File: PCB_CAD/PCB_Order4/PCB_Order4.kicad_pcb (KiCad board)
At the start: 4 copper layers, 150 x 130 mm, 95 parts

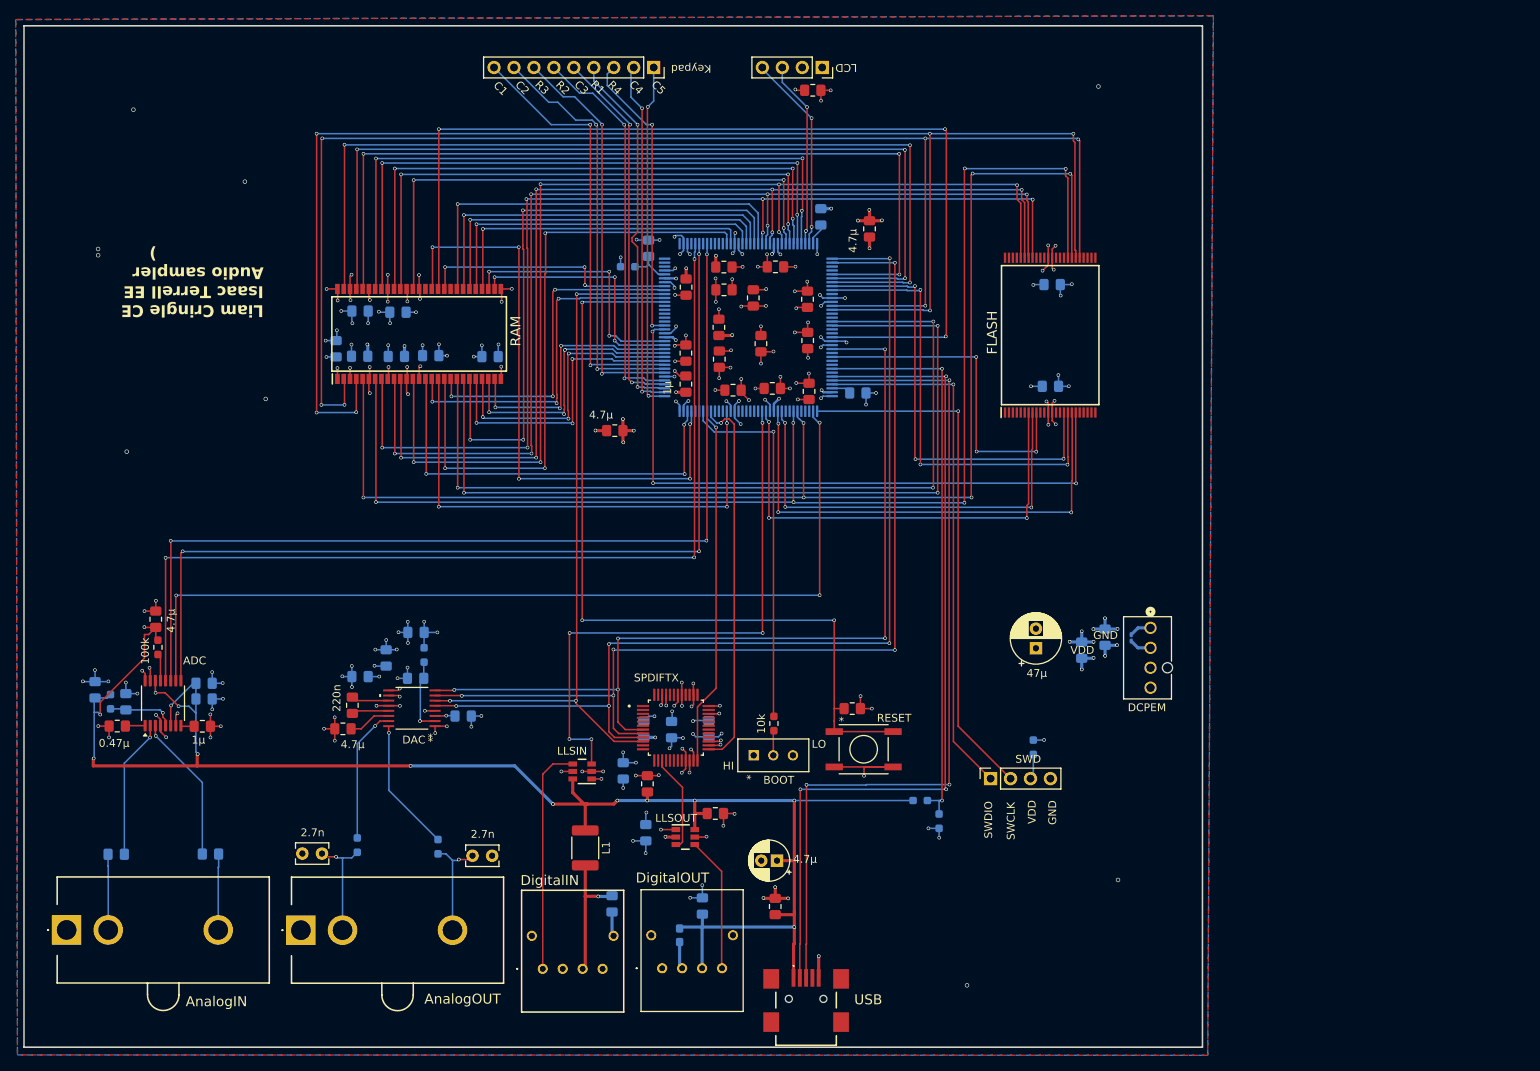
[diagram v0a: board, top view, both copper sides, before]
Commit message: more work on USB and Toslink
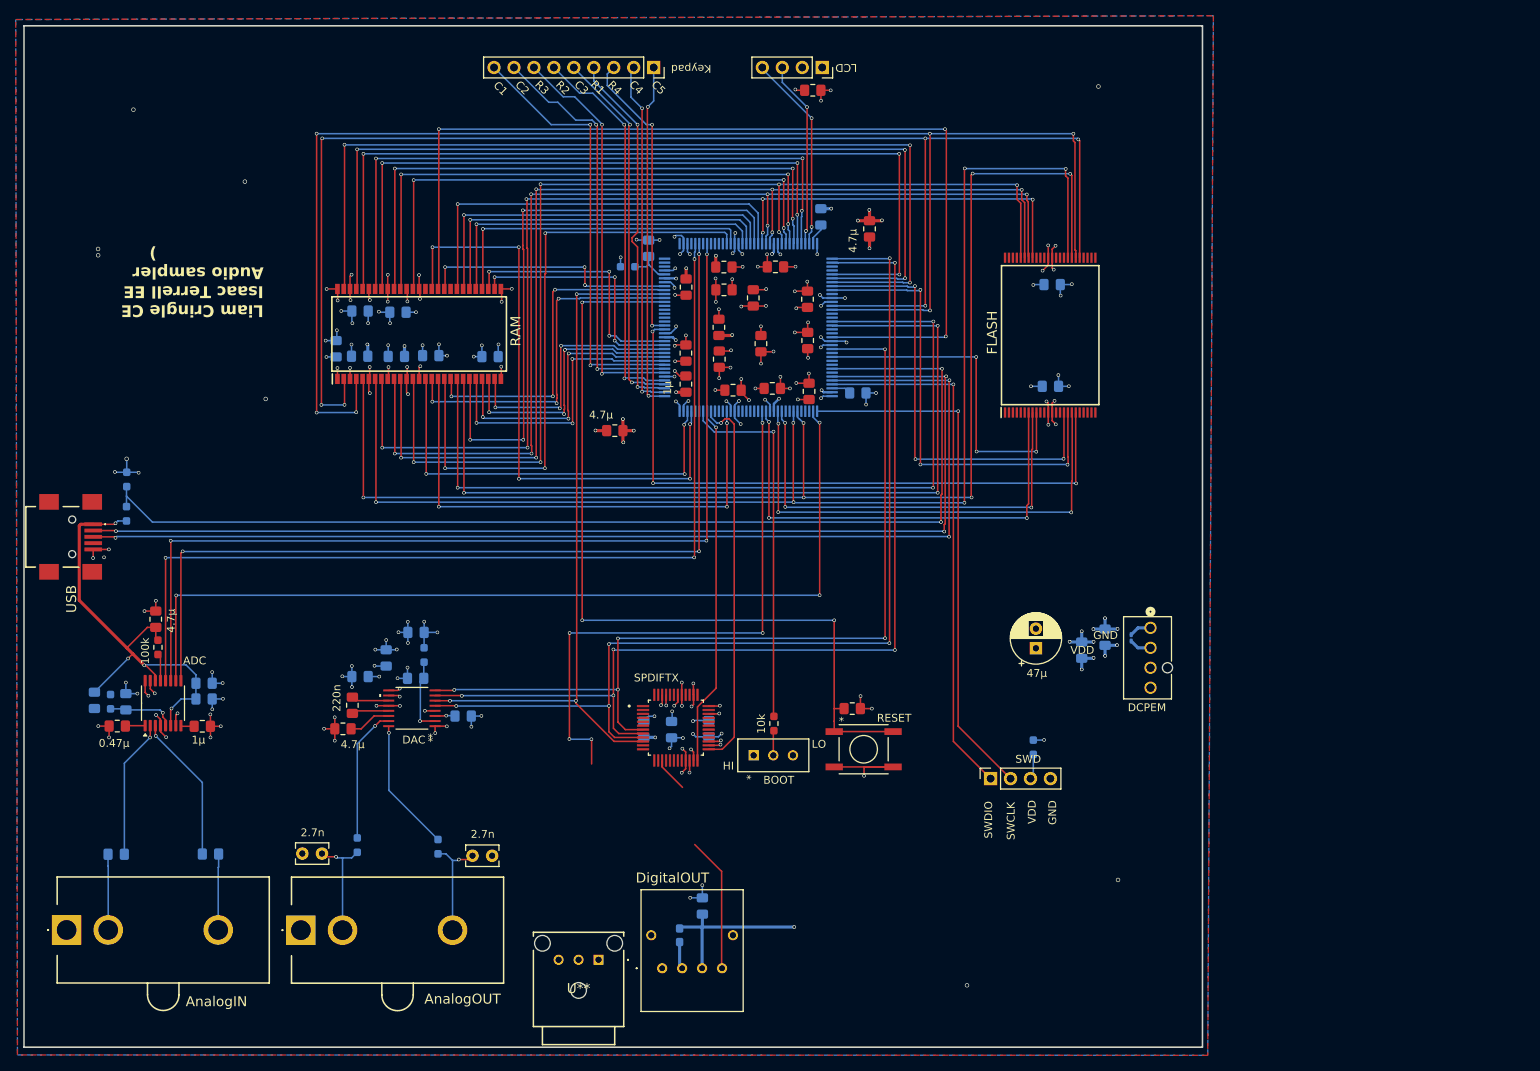
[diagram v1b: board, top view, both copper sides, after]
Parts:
- removed DigitalIN: TORX1950A_F_, CustomModels:TORX1950AF
- removed L1: 47u, Inductor_SMD:L_1812_4532Metric_Pad1.30x3.40mm_HandSolder
- removed LLSC1, LLSC2, LLSC3, LLSC4, TOSLINKC1, USBC1: 0.1u, Capacitor_SMD:C_0805_2012Metric_Pad1.18x1.45mm_HandSolder
- removed LLSIN, LLSOUT: SN74LVC1T45DBVR, CustomModels:TI_LLS_50
- removed USBC2: 4.7u, Capacitor_THT:CP_Radial_D5.0mm_P2.00mm
- added U**: FCR684216R, CustomModels:FCR684216R, F.Cu at (156.6, 139.8)
- moved UR2 112.2 mm to (96.5, 78.6), turned to -90 degrees
- moved USB 111.4 mm to (88.8, 85.9), turned to -90 degrees
- moved UR1 107.4 mm to (96.5, 83.0), turned to -90 degrees
- moved AbC1 1.34 mm to (92.4, 106.8), turned to -90 degrees
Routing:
- net VUSB: track 224.1 -> 81.5 mm, vias 14 -> 5
- net /USB_OTG_HS_VBUS: track 72.5 -> 141.2 mm
- net /USB_OTG_HS_DP: track 109.3 -> 143.9 mm
- net /USB_OTG_HS_DM: track 109.8 -> 142.7 mm
- net /SPDIF_RXOUT: track 29.1 -> 0.00 mm
- net GNDD: track 277.9 -> 251.6 mm, vias 183 -> 167
- net Net-(TOSLINKIN1-VCC): track 16.8 -> 0.00 mm, vias 1 -> 0
- net /SPDIFTX_OUT: track 12.4 -> 4.50 mm
- net VDD: track 120.0 -> 112.6 mm, vias 78 -> 73

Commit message: board work, SWD and boot switches, user IO block
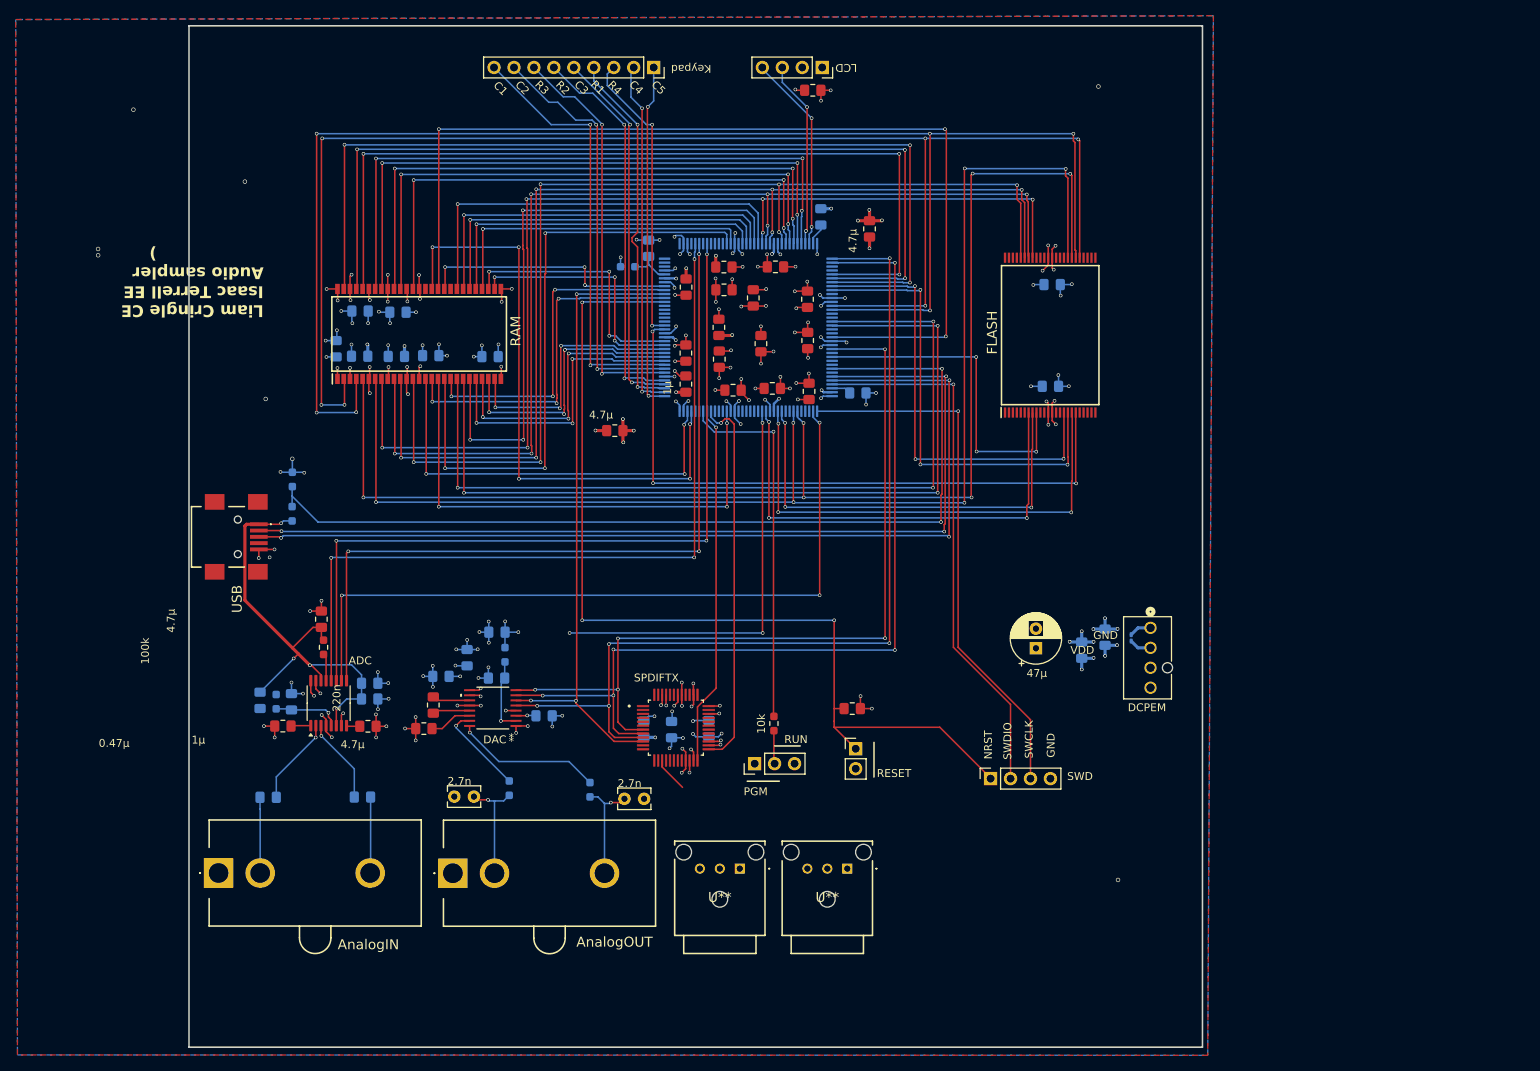
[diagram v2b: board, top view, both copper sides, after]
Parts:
- removed BOOT: SLW-883935-2A-D, CustomModels:SLW-883935_CUD
- removed DigitalOUT: TOTX1950A_F_, CustomModels:TOTX1950AF
- removed the RESET at (190.3, 113.0)
- removed SWDRes: 10k, Resistor_SMD:R_0603_1608Metric_Pad0.98x0.95mm_HandSolder
- removed TOSLINKC2: 0.1u, Capacitor_SMD:C_0805_2012Metric_Pad1.18x1.45mm_HandSolder
- removed TOSLINKR1: 5.6k, Capacitor_SMD:C_0603_1608Metric_Pad1.08x0.95mm_HandSolder
- added REF**: PinHeader_1x03_P2.54mm_Vertical, Connector_PinHeader_2.54mm:PinHeader_1x03_P2.54mm_Vertical, F.Cu at (176.4, 114.8)
- added RESET: PinHeader_1x02_P2.54mm_Vertical, Connector_PinHeader_2.54mm:PinHeader_1x02_P2.54mm_Vertical, F.Cu at (189.3, 112.9)
- added U**: FCR684216T, CustomModels:FCR684216T, F.Cu at (188.2, 128.2)
- moved U** 21.4 mm to (174.6, 128.2)
- moved AbC3 21.1 mm to (121.3, 96.4)
- moved AB1 21.1 mm to (115.5, 106.9)
- moved ADC 21.1 mm to (122.2, 107.1)
- moved AR1 21.1 mm to (121.6, 100.0)
- moved AbC1 21.1 mm to (113.5, 106.8)
- moved AbC2 21.1 mm to (127.5, 104.6)
- moved AcC1 21.1 mm to (116.4, 110.0)
- moved AnC1 21.1 mm to (117.5, 106.9)
- moved AnC2 21.1 mm to (127.5, 106.6)
- moved ArC1 21.1 mm to (127.2, 110.0)
- moved UR1 21.1 mm to (117.6, 83.0)
- moved UR2 21.1 mm to (117.6, 78.6)
- moved USB 21.1 mm to (109.9, 85.9)
- moved AnalogOUT 20.7 mm to (138.0, 128.8)
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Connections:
- SWD pad 1: /DEBUG_SWDIO -> /RST_BTN
- SWD pad 2: /DEBUG_SWCLK -> /DEBUG_SWDIO
- SWD pad 3: SWDVDD -> /DEBUG_SWCLK
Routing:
- net VUSB: track 81.5 -> 59.9 mm, vias 5 -> 4
- net /USB_OTG_HS_VBUS: track 141.2 -> 120.1 mm
- net /I2S1_WS: track 116.6 -> 95.6 mm
- net /I2S1_MCK: track 123.9 -> 102.8 mm
- net /I2S1_CK: track 122.9 -> 101.9 mm
- net /I2S1_SDI: track 121.5 -> 100.4 mm
- net /USB_OTG_HS_DM: track 142.7 -> 121.7 mm
- net /USB_OTG_HS_DP: track 143.9 -> 123.0 mm
- net /SPDIFRX_IN0: track 72.3 -> 52.9 mm, vias 5 -> 3
- net /RST_BTN: track 106.0 -> 124.4 mm
- net /TOSLINKTXIN: track 17.2 -> 0.00 mm
- net GNDD: track 251.6 -> 236.2 mm, vias 167 -> 163
- net /I2S2_SDO: track 91.8 -> 81.5 mm
- net /I2S2_WS: track 130.1 -> 119.8 mm
- net /I2S2_CK: track 130.0 -> 119.7 mm
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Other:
- board size 150 x 130 mm -> 129 x 130 mm
- board text added: "NRST"
- board text added: "PGM"
- board text added: "RUN"
- board text removed: "5.6k"
- board text removed: "HI"
- board text removed: "LO"

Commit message: board work, shrink board, audio IO block, I2C, TVS
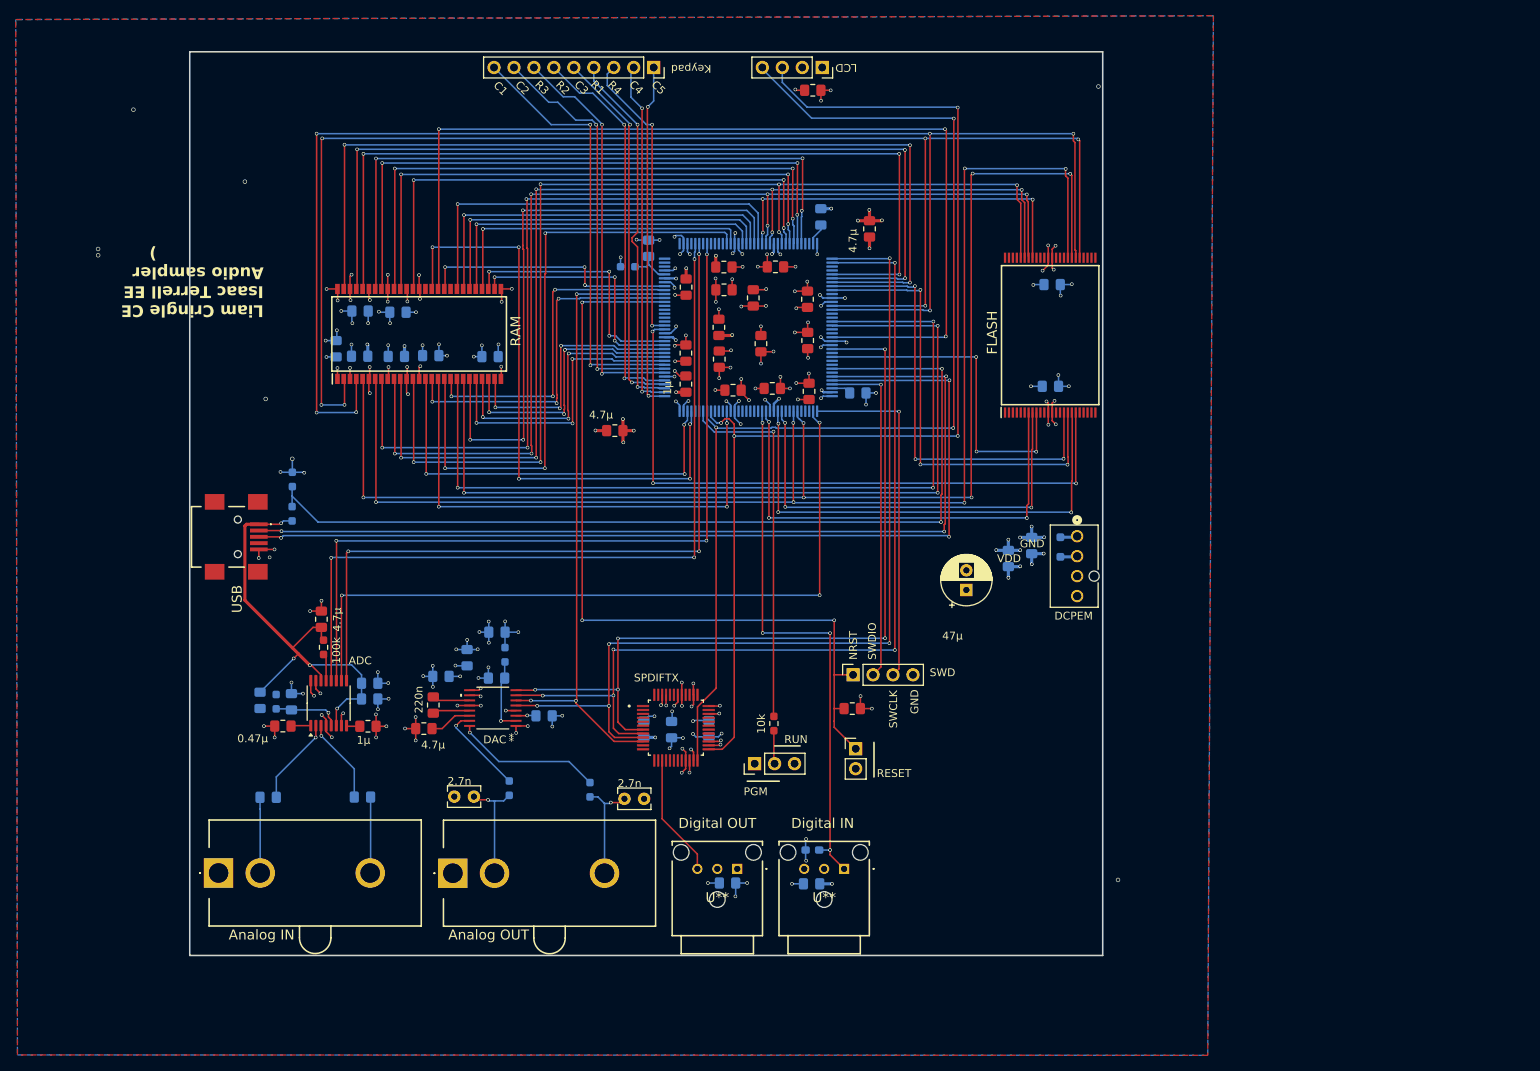
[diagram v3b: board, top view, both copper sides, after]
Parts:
- removed TVS1: DF2S5M4SL_L3F, Diode_SMD:D_0201_0603Metric_Pad0.64x0.40mm_HandSolder
- added REF**: D_SOD-323_HandSoldering, Diode_SMD:D_SOD-323_HandSoldering, B.Cu at (215.4, 87.2)
- added REF**: C_0805_2012Metric_Pad1.18x1.45mm_HandSolder, Capacitor_SMD:C_0805_2012Metric_Pad1.18x1.45mm_HandSolder, B.Cu at (183.7, 130.1)
- added REF**: C_0603_1608Metric_Pad1.08x0.95mm_HandSolder, Capacitor_SMD:C_0603_1608Metric_Pad1.08x0.95mm_HandSolder, B.Cu at (183.8, 125.8)
- added REF**: C_0805_2012Metric_Pad1.18x1.45mm_HandSolder, Capacitor_SMD:C_0805_2012Metric_Pad1.18x1.45mm_HandSolder, B.Cu at (173.0, 130.0)
- Analog IN: renamed from AnalogIN
- Analog OUT: renamed from AnalogOUT
- moved SWD 21.9 mm to (189.0, 103.5)
- moved PEC1 14.9 mm to (208.7, 88.7)
- moved DCPEM 14.9 mm to (217.5, 85.9)
- moved PEC2 14.9 mm to (211.7, 87.0)
- moved U** 14.0 mm to (174.2, 128.2)
- moved U** 13.3 mm to (187.8, 128.2)
- moved PEC3 11.6 mm to (203.4, 92.7)
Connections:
- LCD pad 3: /I2C2_SCL -> /I2C1_SCL
- LCD pad 4: /I2C2_SDA -> /I2C1_SDA
- Microcontroller pad 69: /I2C2_SCL -> (no net)
- Microcontroller pad 70: /I2C2_SDA -> (no net)
- U** pad 1: (no net) -> /SPDIFRX_IN0
- U** pad 2: (no net) -> GNDD
- U** pad 3: (no net) -> VDD
- U** pad 1: (no net) -> GNDD
- U** pad 2: (no net) -> VDD
- U** pad 3: (no net) -> /SPDIFTX_OUT
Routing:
- net /I2C1_SDA: track 45.9 -> 142.8 mm, vias 1 -> 3
- net /I2C1_SCL: track 48.3 -> 144.1 mm, vias 1 -> 4
- net /I2C2_SDA: track 25.1 -> 0.00 mm, vias 2 -> 0
- net /DEBUG_SWDIO: track 68.6 -> 43.6 mm
- net /DEBUG_SWCLK: track 68.5 -> 44.3 mm
- net /I2C2_SCL: track 23.8 -> 0.00 mm, vias 2 -> 0
- net /RST_BTN: track 124.4 -> 104.2 mm
- net /SPDIFRX_IN0: track 52.9 -> 69.0 mm, vias 3 -> 4
- net /SPDIFTX_OUT: track 4.50 -> 15.7 mm
- net GNDD: track 236.2 -> 243.3 mm, vias 163 -> 168
- net VDD: track 111.3 -> 113.7 mm, vias 72 -> 74
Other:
- board size 129 x 130 mm -> 116.2 x 115 mm
- board text added: "Digital IN"
- board text added: "Digital OUT"

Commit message: board work mostly minor cleanup. starting DIX9211 rerouting soon
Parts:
- removed PEC1, PEC2: 1u, Capacitor_SMD:C_0805_2012Metric_Pad1.18x1.45mm_HandSolder
- added REF**: R_0603_1608Metric_Pad0.98x0.95mm_HandSolder, Resistor_SMD:R_0603_1608Metric_Pad0.98x0.95mm_HandSolder, B.Cu at (188.7, 71.1)
- added REF**: R_0603_1608Metric_Pad0.98x0.95mm_HandSolder, Resistor_SMD:R_0603_1608Metric_Pad0.98x0.95mm_HandSolder, B.Cu at (188.8, 75.2)
- moved LnC1 1.12 mm to (184.8, 29.7), turned to 0 degrees
- moved MnC5 0.35 mm to (178.7, 66.7)
- turned PEC3 to -90 degrees
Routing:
- net GNDD: track 243.3 -> 234.4 mm, vias 168 -> 161
- net VDD: track 113.7 -> 110.8 mm, vias 74 -> 72
- net /I2C1_SDA: track 142.8 -> 143.8 mm
- net /I2C1_SCL: track 144.1 -> 145.1 mm, vias 4 -> 5
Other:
- board text added: "4.7k"

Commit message: board work, move debug block in preparation for rewiring DIX9211. GPIO pin for SPDIF error interrupt will be 111, but didn't update CubeMX
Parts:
- removed DXnC1, DXnC2, DXnC3: 0.1u, Capacitor_SMD:C_0805_2012Metric_Pad1.18x1.45mm_HandSolder
- BC1: moved to B.Cu
- moved REF** 27.2 mm to (210.9, 130.1)
- moved REF** 27.2 mm to (211.0, 125.8)
- moved REF** 27.2 mm to (200.2, 130.0)
- moved U** 27.2 mm to (215.0, 128.2)
- moved U** 27.2 mm to (201.4, 128.2)
- moved REF** 26.5 mm to (202.9, 115.9)
- moved SR1 26.5 mm to (205.4, 110.8)
- moved RESET 23.7 mm to (213.0, 113.2)
- moved SWD 19.8 mm to (208.8, 103.4)
- moved BC1 16.5 mm to (205.3, 105.9), turned to -90 degrees
- moved SPDIFTX 9.54 mm to (174.4, 115.5), turned to -90 degrees
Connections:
- Microcontroller pad 111: unconnected-(uController1-PC10-Pad111) -> SPDIF_ERR
- SPDIFTX pad 1: unconnected-(SPDIFTX1-ERROR/INT0-Pad1) -> SPDIF_ERR
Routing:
- net /I2C1_SDA: track 143.8 -> 100.4 mm
- net /I2C1_SCL: track 145.1 -> 102.8 mm
- net /SPDIFRX_IN0: track 69.0 -> 38.2 mm
- net /BOOTSW: track 47.0 -> 75.4 mm
- net GNDD: track 234.4 -> 208.6 mm, vias 161 -> 144
- net /RST_BTN: track 104.2 -> 125.3 mm, vias 3 -> 4
- net /DEBUG_SWCLK: track 44.3 -> 62.8 mm, vias 1 -> 3
- net /DEBUG_SWDIO: track 43.6 -> 61.9 mm, vias 1 -> 3
- net /SPDIFTX_OUT: track 15.7 -> 0.00 mm
- net VDD: track 110.8 -> 99.9 mm, vias 72 -> 65
- net /I2S2_SDO: track 81.5 -> 70.9 mm
- net /I2S2_CK: track 119.7 -> 111.5 mm
- net /I2S2_WS: track 119.8 -> 111.9 mm
- net /I2S2_MCK: track 104.9 -> 97.1 mm
